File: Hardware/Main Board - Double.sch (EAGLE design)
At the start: 75 parts, among them J1 MICROMOD-2222-C, J10 MICRO-SD-PUSH-PUSH-EXT-PIN, J2 Vertical Qwiic Connector, J4 QWIIC_RIGHT_ANGLE, J5 CORTEX_JTAG_DEBUG_MINIMUM_PTH, J6 MICROMOD_FUNCTION_MAIN, J7 MICROMOD_FUNCTION_MAIN, Q1 3.1A/30V/105mΩ, U1 STG3856QTR, U2 MCP73831, U5 AP7361C-33

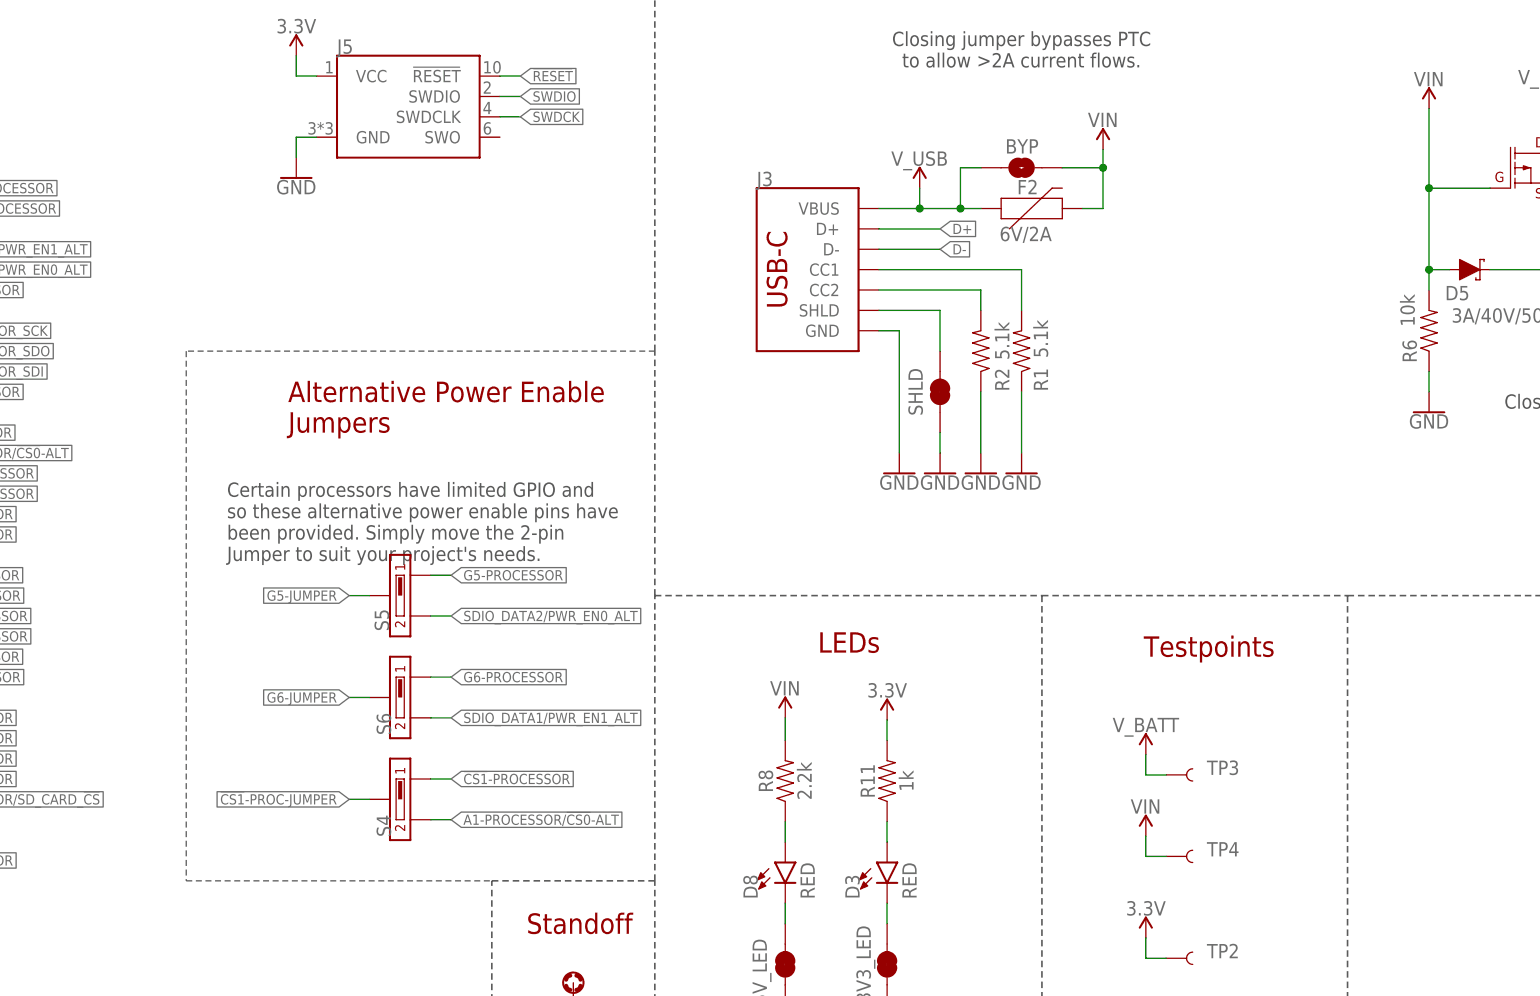
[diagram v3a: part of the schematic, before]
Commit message: Adds ESD protection to USB lines, replaces switches with cheaper more widely available ones
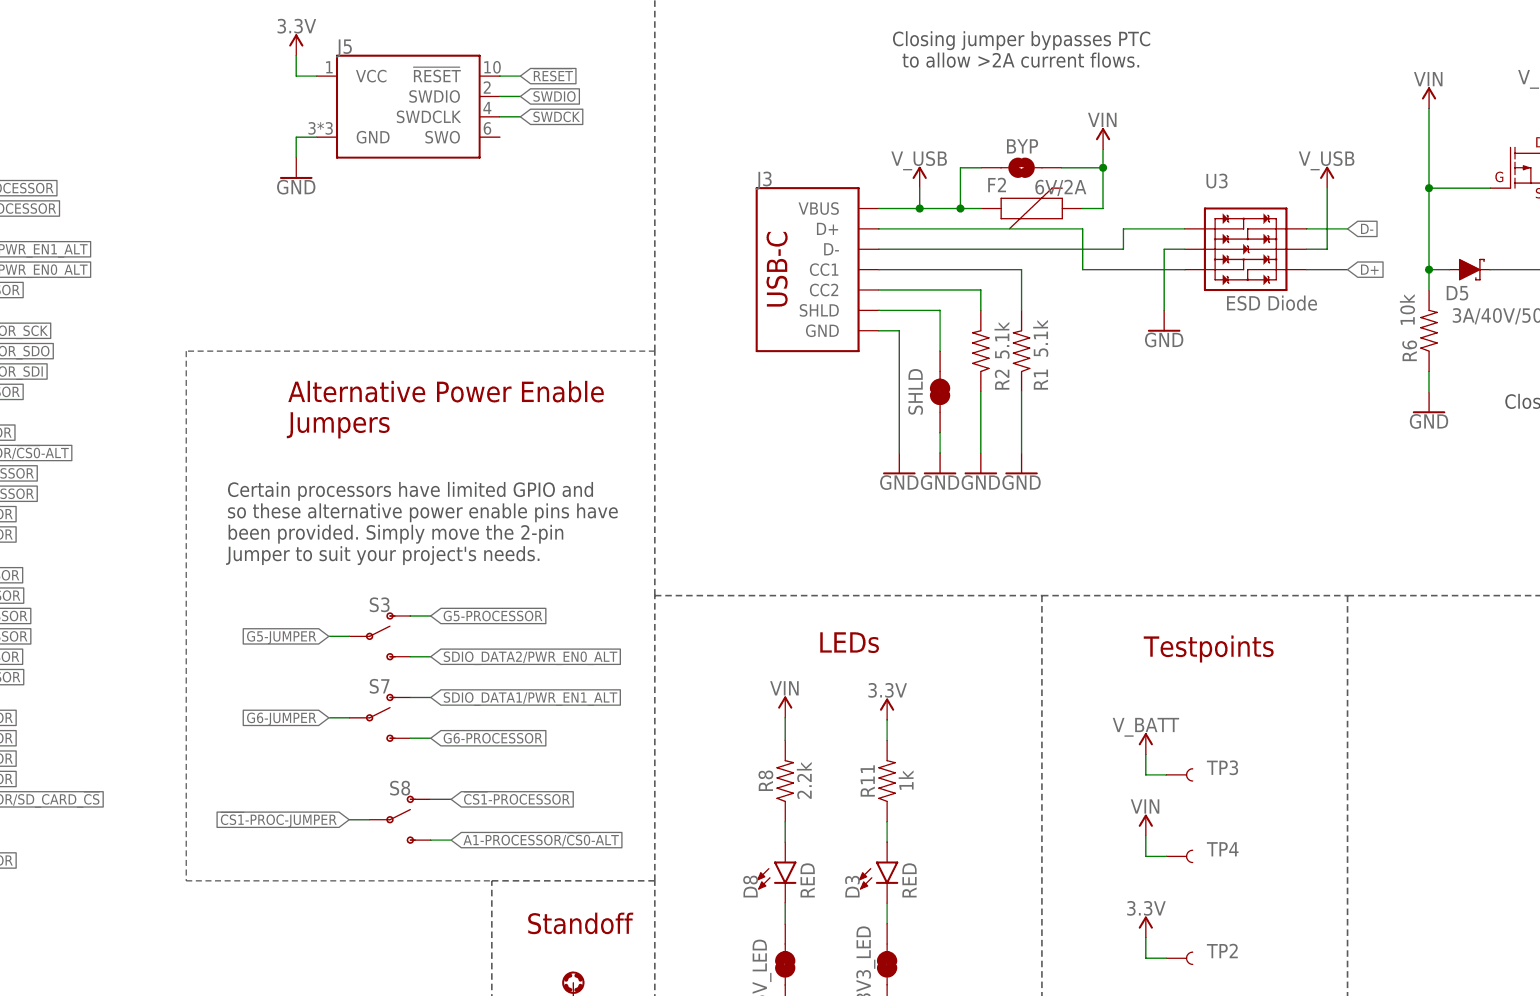
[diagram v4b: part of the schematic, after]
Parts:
- removed S4, S5, S6: DIPSWITCH-3-PIN, dip_switch:DIPSWITCH-3-PIN
- added S3, S7, S8: (no value), SparkFun-Switches:SWITCH-SPDT-SMD-RIGHT-ANGLE
- added U3: ESD Diode, SparkFun-DiscreteSemi:TVS_DIODE_ARRAYSMD
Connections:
- new net N$7: J3.D+, U3.IO2
- new net N$8: J3.D-, U3.IO1
- net !CS1!-PROC-JUMPER: now also S8.P; no longer S4.2
- net !CS1!-PROCESSOR: now also S8.O; no longer S4.3
- net A1-PROCESSOR/!CS0!-ALT: now also S8.S; no longer S4.1
- net D+: now also U3.IO3; no longer J3.D+
- net D-: now also U3.IO4; no longer J3.D-
- net G5-JUMPER: now also S3.P; no longer S5.2
- net G5-PROCESSOR: now also S3.O; no longer S5.3
- net G6-JUMPER: now also S7.P; no longer S6.2
- net G6-PROCESSOR: now also S7.S; no longer S6.3
- net GND: now also U3.VSS
- net SDIO_DATA1/PWR_EN1_ALT: now also S7.O; no longer S6.1
- net SDIO_DATA2/PWR_EN0_ALT: now also S3.S; no longer S5.1
- net V_USB: now also U3.VCC

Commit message: Adds new VREG, new VREG added to control 3.3V @ Qwiic Connectors, moves i2c pullup jumper (connected to 3v3 not 3v3_Qwiic)
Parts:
- added C1, C2: 1.0uF, SparkFun-Capacitors:1.0UF-0603-16V-10%
- added R4: 100k, SparkFun-Resistors:100KOHM-0603-1/10W-1%
- added U4: 3.3V, dip_switch:V_REG_AP7347DQK-3.3V
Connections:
- removed net I2C_SCL1-PROCESSOR: J1.I2C_SCL1
- removed net I2C_SDA1-PROCESSOR: J1.I2C_SDA1
- new net 3.3V_QWIIC: C1.1, J2.2, J4.2, U4.OUT
- new net I2C_SCL1-PROCESSOR/QWIIC_EN: J1.I2C_SCL1, R4.1, U4.EN
- net 3.3V: no longer J2.2, J4.2
- net GND: now also C1.2, C2.2, U4.GND
- net VCC: now also C2.1, R4.2, U4.IN
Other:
- moved on the sheet: C3, C4, D4, D5, J8, Q1, R10, R3, R5, R6, R7, U2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

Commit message: Adds silk, updates alignment of existing silk that was not replaced, updates landing pads for new mux part
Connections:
- net A1-PROCESSOR/!CS0!-ALT renamed A1-PROCESSOR/!CS1!-ALT
- net RX1-AUX_TX-FC0-PLEX renamed RX1-DFU_TX-FC0-PLEX
- net RX1-AUX_TX-FC1-PLEX renamed RX1-DFU_TX-FC1-PLEX
- net TX1-AUX_RX-FC0-PLEX renamed TX1-DFU_RX-FC0-PLEX
- net TX1-AUX_RX-FC1-PLEX renamed TX1-DFU_RX-FC1-PLEX
- net G6-PROCESSOR: now also S7.O; no longer S7.S
- net SDIO_DATA1/PWR_EN1_ALT: now also S7.S; no longer S7.O
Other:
- moved on the sheet: I2C_PU
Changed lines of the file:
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@@
 <attribute name="VALUE" x="43.18" y="251.714" size="1.778" layer="96" font="vector" align="bottom-center"/>
 </instance>
-<instance part="GND4" gate="1" x="25.4" y="38.1" smashed="yes">
-<attribute name="VALUE" x="25.4" y="37.846" size="1.778" layer="96" font="vector" align="top-center"/>
-</instance>
-<instance part="GND5" gate="1" x="116.84" y="38.1" smashed="yes">
-<attribute name="VALUE" x="116.84" y="37.846" size="1.778" layer="96" font="vector" align="top-center"/>
+<instance part="GND4" gate="1" x="25.4" y="43.18" smashed="yes">
+<attribute name="VALUE" x="25.4" y="42.926" size="1.778" layer="96" font="vector" align="top-center"/>
+</instance>
+<instance part="GND5" gate="1" x="116.84" y="43.18" smashed="yes">
+<attribute name="VALUE" x="116.84" y="42.926" size="1.778" layer="96" font="vector" align="top-center"/>
 </instance>
 <instance part="GND7" gate="1" x="43.18" y="147.32" smashed="yes">
@@
 <instance part="LOGO2" gate="G$1" x="330.2" y="33.02" smashed="yes"/>
 <instance part="LOGO3" gate="G$1" x="419.1" y="45.72" smashed="yes"/>
-<instance part="SUPPLY1" gate="G$1" x="27.94" y="231.14" smashed="yes">
-<attribute name="VALUE" x="27.94" y="233.934" size="1.778" layer="96" align="bottom-center"/>
+<instance part="SUPPLY1" gate="G$1" x="33.02" y="248.92" smashed="yes">
+<attribute name="VALUE" x="33.02" y="251.714" size="1.778" layer="96" align="bottom-center"/>
 </instance>
 <instance part="J8" gate="G$1" x="353.06" y="167.64" smashed="yes" rot="MR90">
@@
 <attribute name="VALUE" x="210.82" y="56.134" size="1.778" layer="96" font="vector" align="bottom-center"/>
 </instance>
-<instance part="I2C_PU" gate="G$1" x="414.02" y="93.98" smashed="yes" rot="R180">
-<attribute name="NAME" x="408.432" y="93.98" size="1.778" layer="95" font="vector" align="center"/>
+<instance part="I2C_PU" gate="G$1" x="411.48" y="93.98" smashed="yes" rot="R180">
+<attribute name="NAME" x="405.892" y="93.98" size="1.778" layer="95" font="vector" align="center"/>
 </instance>
 <instance part="R14" gate="G$1" x="403.86" y="101.6" smashed="yes">
@@
 <attribute name="VALUE" x="256.54" y="231.14" size="1.778" layer="96"/>
 </instance>
-<instance part="GND24" gate="1" x="248.92" y="228.6" smashed="yes" rot="MR0">
-<attribute name="VALUE" x="248.92" y="228.346" size="1.778" layer="96" font="vector" rot="MR0" align="top-center"/>
+<instance part="GND24" gate="1" x="248.92" y="231.14" smashed="yes" rot="MR0">
+<attribute name="VALUE" x="248.92" y="230.886" size="1.778" layer="96" font="vector" rot="MR0" align="top-center"/>
 </instance>
 <instance part="SUPPLY31" gate="G$1" x="269.24" y="246.38" smashed="yes">
@@
 <attribute name="VALUE" x="398.78" y="157.226" size="1.778" layer="96" font="vector" align="top-left"/>
 </instance>
-<instance part="GND22" gate="1" x="393.7" y="149.86" smashed="yes">
-<attribute name="VALUE" x="393.7" y="149.606" size="1.778" layer="96" font="vector" align="top-center"/>
+<instance part="GND22" gate="1" x="393.7" y="152.4" smashed="yes">
+<attribute name="VALUE" x="393.7" y="152.146" size="1.778" layer="96" font="vector" align="top-center"/>
 </instance>
 <instance part="SUPPLY32" gate="G$1" x="378.46" y="172.72" smashed="yes">
@@
 <attribute name="VALUE" x="378.46" y="152.146" size="1.778" layer="96" font="vector" align="top-center"/>
 </instance>
-<instance part="GND29" gate="1" x="419.1" y="157.48" smashed="yes">
-<attribute name="VALUE" x="419.1" y="157.226" size="1.778" layer="96" font="vector" align="top-center"/>
+<instance part="GND29" gate="1" x="419.1" y="152.4" smashed="yes">
+<attribute name="VALUE" x="419.1" y="152.146" size="1.778" layer="96" font="vector" align="top-center"/>
 </instance>
 <instance part="R4" gate="G$1" x="388.62" y="162.56" smashed="yes" rot="R90">
@@
 <attribute name="VALUE" x="370.84" y="89.154" size="1.778" layer="96" align="bottom-center"/>
 </instance>
-<instance part="SUPPLY29" gate="G$1" x="421.64" y="96.52" smashed="yes">
-<attribute name="VALUE" x="421.64" y="99.314" size="1.778" layer="96" font="vector" align="bottom-center"/>
+<instance part="SUPPLY29" gate="G$1" x="419.1" y="96.52" smashed="yes">
+<attribute name="VALUE" x="419.1" y="99.314" size="1.778" layer="96" font="vector" align="bottom-center"/>
 </instance>
 </instances>
@@
 <segment>
 <pinref part="I2C_PU" gate="G$1" pin="2"/>
-<wire x1="421.64" y1="93.98" x2="419.1" y2="93.98" width="0.1524" layer="91"/>
+<wire x1="419.1" y1="93.98" x2="416.56" y2="93.98" width="0.1524" layer="91"/>
 <pinref part="SUPPLY29" gate="G$1" pin="3.3V"/>
-<wire x1="421.64" y1="93.98" x2="421.64" y2="96.52" width="0.1524" layer="91"/>
+<wire x1="419.1" y1="93.98" x2="419.1" y2="96.52" width="0.1524" layer="91"/>
 </segment>
 </net>
@@
 <pinref part="GND4" gate="1" pin="GND"/>
 <wire x1="27.94" y1="48.26" x2="25.4" y2="48.26" width="0.1524" layer="91"/>
-<wire x1="25.4" y1="48.26" x2="25.4" y2="40.64" width="0.1524" layer="91"/>
+<wire x1="25.4" y1="48.26" x2="25.4" y2="45.72" width="0.1524" layer="91"/>
 <wire x1="27.94" y1="60.96" x2="25.4" y2="60.96" width="0.1524" layer="91"/>
 <wire x1="25.4" y1="60.96" x2="25.4" y2="58.42" width="0.1524" layer="91"/>
@@
 <pinref part="GND5" gate="1" pin="GND"/>
 <wire x1="119.38" y1="48.26" x2="116.84" y2="48.26" width="0.1524" layer="91"/>
-<wire x1="116.84" y1="48.26" x2="116.84" y2="40.64" width="0.1524" layer="91"/>
+<wire x1="116.84" y1="48.26" x2="116.84" y2="45.72" width="0.1524" layer="91"/>
 <junction x="116.84" y="48.26"/>
 <wire x1="116.84" y1="55.88" x2="116.84" y2="48.26" width="0.1524" layer="91"/>
@@
 <pinref part="U3" gate="U1" pin="VSS"/>
 <wire x1="251.46" y1="238.76" x2="248.92" y2="238.76" width="0.1524" layer="91"/>
-<wire x1="248.92" y1="238.76" x2="248.92" y2="231.14" width="0.1524" layer="91"/>
+<wire x1="248.92" y1="238.76" x2="248.92" y2="233.68" width="0.1524" layer="91"/>
 <pinref part="GND24" gate="1" pin="GND"/>
 </segment>
 <segment>
 <pinref part="U4" gate="G$1" pin="GND"/>
-<wire x1="393.7" y1="152.4" x2="393.7" y2="165.1" width="0.1524" layer="91"/>
+<wire x1="393.7" y1="154.94" x2="393.7" y2="165.1" width="0.1524" layer="91"/>
 <wire x1="393.7" y1="165.1" x2="396.24" y2="165.1" width="0.1524" layer="91"/>
 <pinref part="GND22" gate="1" pin="GND"/>
@@
 <pinref part="GND29" gate="1" pin="GND"/>
 <pinref part="C1" gate="G$1" pin="2"/>
+<wire x1="419.1" y1="154.94" x2="419.1" y2="160.02" width="0.1524" layer="91"/>
 </segment>
 </net>
@@
 </segment>
 <segment>
-<label x="160.02" y="182.88" size="1.27" layer="95" font="vector" xref="yes"/>
-<wire x1="157.48" y1="182.88" x2="160.02" y2="182.88" width="0.1524" layer="91"/>
-<pinref part="S7" gate="1" pin="O"/>
+<label x="160.02" y="177.8" size="1.27" layer="95" font="vector" xref="yes"/>
+<wire x1="157.48" y1="177.8" x2="160.02" y2="177.8" width="0.1524" layer="91"/>
+<pinref part="S7" gate="1" pin="S"/>
 </segment>
 </net>
@@
 </segment>
 </net>
-<net name="A1-PROCESSOR/!CS0!-ALT" class="0">
+<net name="A1-PROCESSOR/!CS1!-ALT" class="0">
 <segment>
 <pinref part="J1" gate="J1" pin="A1"/>
@@
 </segment>
 <segment>
-<label x="160.02" y="177.8" size="1.27" layer="95" font="vector" xref="yes"/>
-<wire x1="157.48" y1="177.8" x2="160.02" y2="177.8" width="0.1524" layer="91"/>
-<pinref part="S7" gate="1" pin="S"/>
+<label x="160.02" y="182.88" size="1.27" layer="95" font="vector" xref="yes"/>
+<wire x1="157.48" y1="182.88" x2="160.02" y2="182.88" width="0.1524" layer="91"/>
+<pinref part="S7" gate="1" pin="O"/>
 </segment>
 </net>
@@
 <segment>
 <pinref part="J1" gate="J1" pin="USB_VIN"/>
-<wire x1="45.72" y1="228.6" x2="27.94" y2="228.6" width="0.1524" layer="91"/>
-<wire x1="27.94" y1="228.6" x2="27.94" y2="231.14" width="0.1524" layer="91"/>
+<wire x1="45.72" y1="228.6" x2="33.02" y2="228.6" width="0.1524" layer="91"/>
+<wire x1="33.02" y1="228.6" x2="33.02" y2="248.92" width="0.1524" layer="91"/>
 <pinref part="SUPPLY1" gate="G$1" pin="VIN"/>
 </segment>
@@
 </segment>
 </net>
-<net name="TX1-AUX_RX-FC0-PLEX" class="0">
+<net name="TX1-DFU_RX-FC0-PLEX" class="0">
 <segment>
 <wire x1="25.4" y1="86.36" x2="27.94" y2="86.36" width="0.1524" layer="91"/>
@@
 </segment>
 </net>
-<net name="RX1-AUX_TX-FC1-PLEX" class="0">
+<net name="RX1-DFU_TX-FC1-PLEX" class="0">
 <segment>
 <wire x1="116.84" y1="88.9" x2="119.38" y2="88.9" width="0.1524" layer="91"/>
@@
 </segment>
 </net>
-<net name="RX1-AUX_TX-FC0-PLEX" class="0">
+<net name="RX1-DFU_TX-FC0-PLEX" class="0">
 <segment>
 <wire x1="25.4" y1="88.9" x2="27.94" y2="88.9" width="0.1524" layer="91"/>
@@
 </segment>
 </net>
-<net name="TX1-AUX_RX-FC1-PLEX" class="0">
+<net name="TX1-DFU_RX-FC1-PLEX" class="0">
 <segment>
 <wire x1="116.84" y1="86.36" x2="119.38" y2="86.36" width="0.1524" layer="91"/>
@@
 <segment>
 <pinref part="I2C_PU" gate="G$1" pin="3"/>
-<wire x1="414.02" y1="99.06" x2="414.02" y2="101.6" width="0.1524" layer="91"/>
-<wire x1="414.02" y1="101.6" x2="408.94" y2="101.6" width="0.1524" layer="91"/>
+<wire x1="411.48" y1="99.06" x2="411.48" y2="101.6" width="0.1524" layer="91"/>
+<wire x1="411.48" y1="101.6" x2="408.94" y2="101.6" width="0.1524" layer="91"/>
 <pinref part="R14" gate="G$1" pin="2"/>
 </segment>
@@
 <segment>
 <pinref part="I2C_PU" gate="G$1" pin="1"/>
-<wire x1="414.02" y1="88.9" x2="414.02" y2="86.36" width="0.1524" layer="91"/>
-<wire x1="414.02" y1="86.36" x2="408.94" y2="86.36" width="0.1524" layer="91"/>
+<wire x1="411.48" y1="88.9" x2="411.48" y2="86.36" width="0.1524" layer="91"/>
+<wire x1="411.48" y1="86.36" x2="408.94" y2="86.36" width="0.1524" layer="91"/>
 <pinref part="R15" gate="G$1" pin="2"/>
 </segment>
